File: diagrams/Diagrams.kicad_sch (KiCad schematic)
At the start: 16 parts

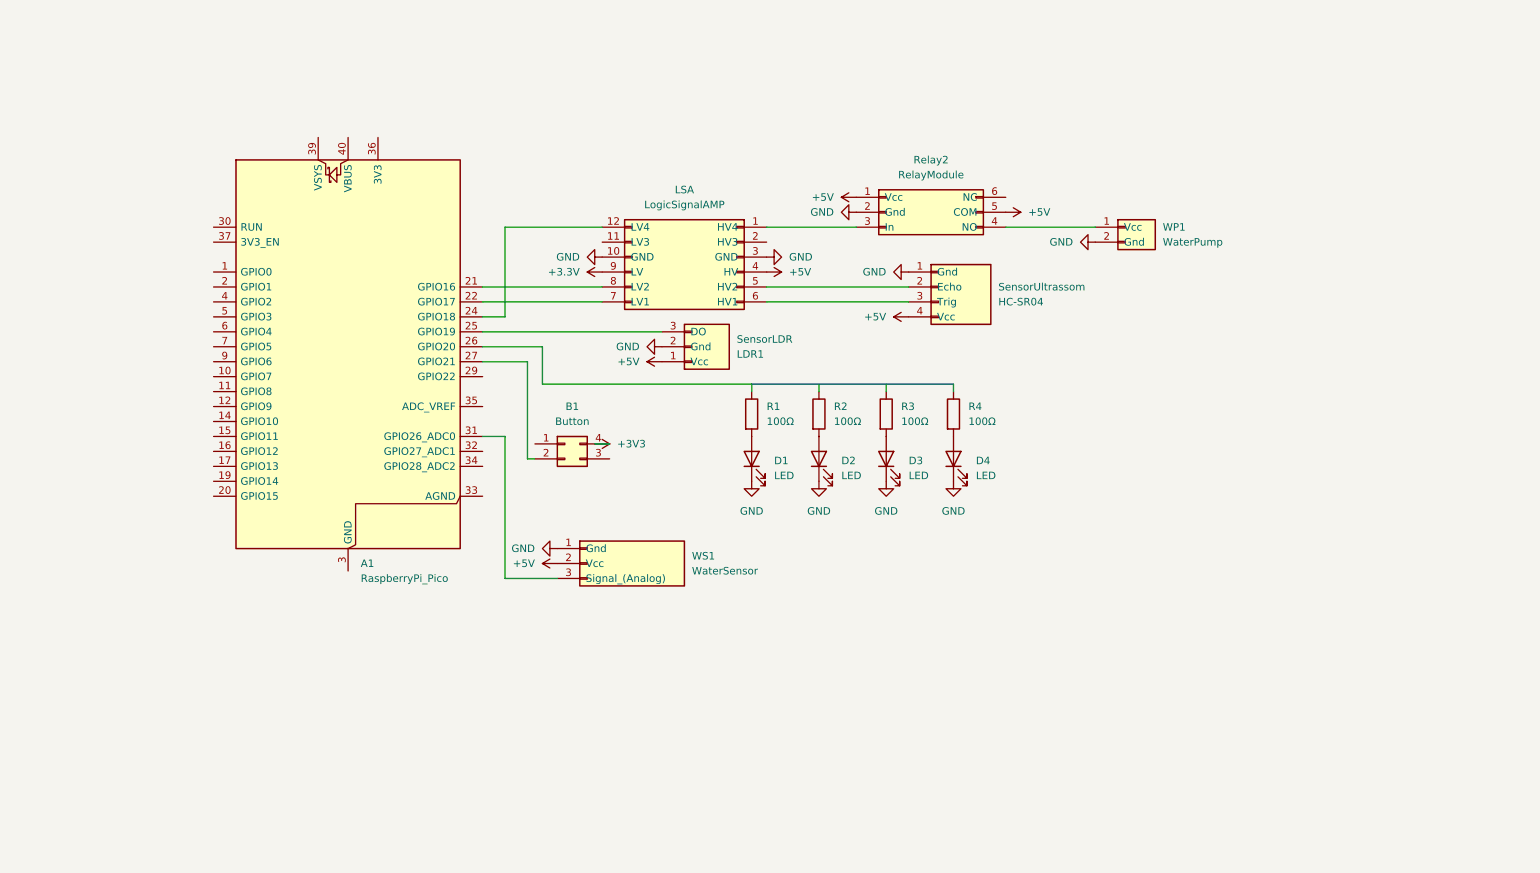
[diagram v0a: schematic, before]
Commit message: update: diagramas
- alterações pequenas no diagrama esquemático
- diagrama pcb inicial implementado
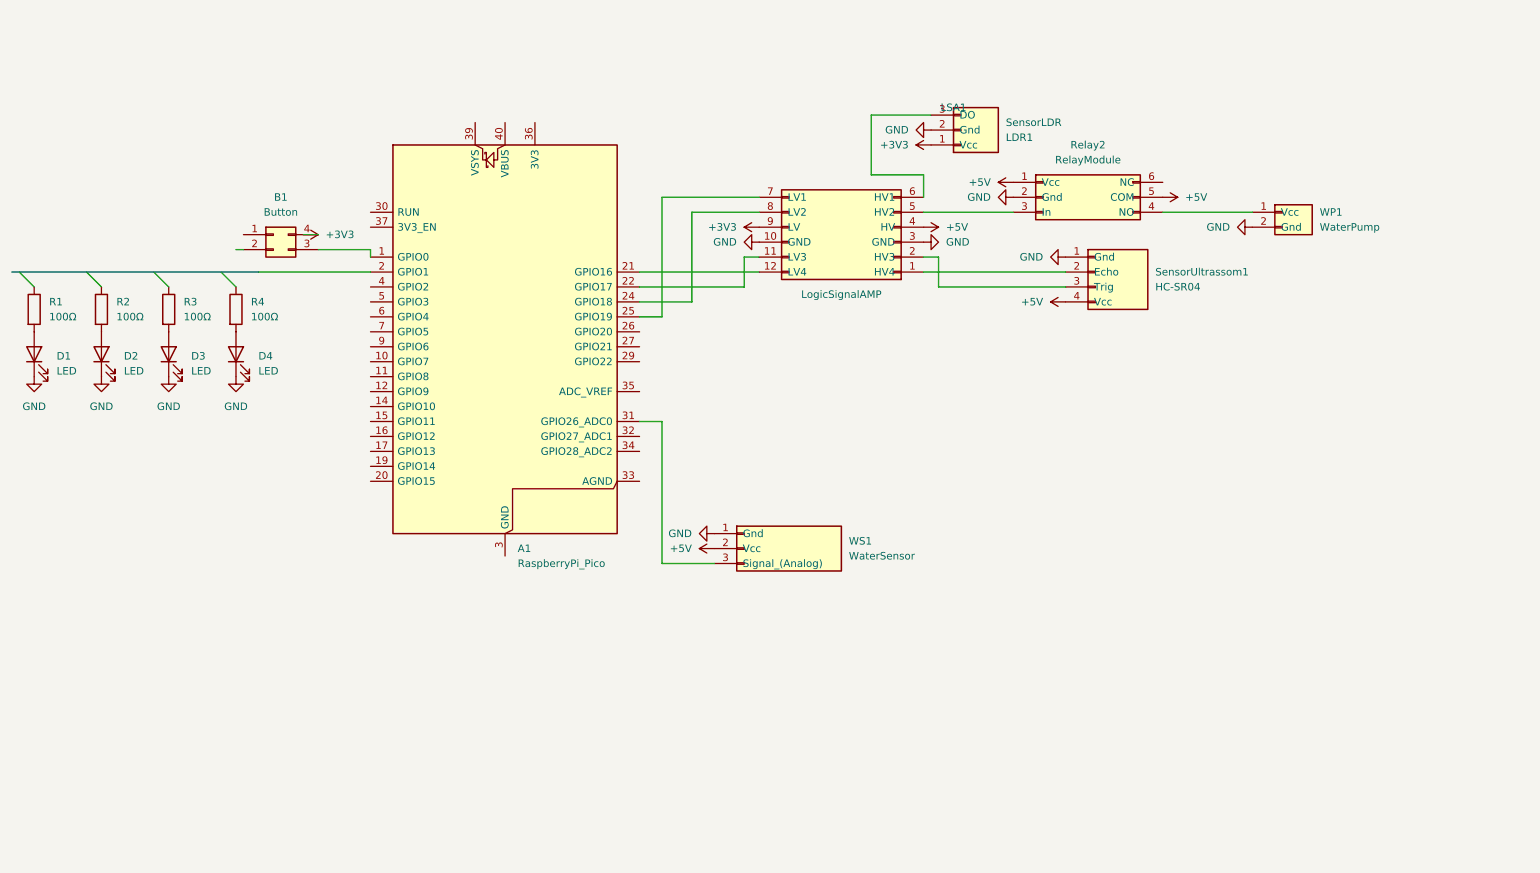
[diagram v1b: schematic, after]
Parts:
- renumbered LSA to LSA1, SensorUltrassom to SensorUltrassom1
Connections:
- net +3.3V is gone; now on net +3V3: LSA1.9 (LV)
- net +3V3: now also LDR1.1 (Vcc)
- net +5V: no longer LDR1.1 (Vcc)
- net at R1.1: no longer A1.26 (GPIO20)
- net at A1.1 (GPIO0): now also B1.3 (Pin_3)
- net at A1.21 (GPIO16): now also LSA1.12 (LV4); no longer LSA1.8 (LV2)
- net at A1.22 (GPIO17): now also LSA1.11 (LV3); no longer LSA1.7 (LV1)
- net at A1.24 (GPIO18): now also LSA1.8 (LV2); no longer LSA1.12 (LV4)
- net at A1.25 (GPIO19): now also LSA1.7 (LV1); no longer LDR1.3 (DO)
- net at A1.27 (GPIO21): no longer B1.2 (Pin_2)
- net at LSA1.1 (HV4): now also SensorUltrassom1.2 (Echo); no longer Relay2.3 (In)
- net at LSA1.2 (HV3): now also SensorUltrassom1.3 (Trig)
- net at LSA1.5 (HV2): now also Relay2.3 (In); no longer SensorUltrassom1.2 (Echo)
- net at LSA1.6 (HV1): now also LDR1.3 (DO); no longer SensorUltrassom1.3 (Trig)
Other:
- moved on the sheet: A1, B1, D1, D2, D3, D4, LDR1, LSA1, R1, R2, R3, R4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

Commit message: update: novo esquemático
- Esquemático refeito
- Nova biblioteca adicionada
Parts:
- removed LDR1: SensorLDR, symbol Connector_Generic:Conn_01x03
- added LDR: Conn_01x03_Socket, symbol Connector:Conn_01x03_Socket
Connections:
- net +5V: now also A1.40 (VBUS), LDR.1 (5V)
- net GND: now also A1.13 (GND), A1.18 (GND), A1.23 (GND), A1.28 (GND), A1.3 (GND), A1.38 (GND), A1.8 (GND), LDR.2 (GND)
- net HV1: now reaches LSA1.6 (HV1)
- net HV1: now also LDR.3 (LDR_SIGNAL)
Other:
- moved on the sheet: Relay2, SensorUltrassom1, WP1

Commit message: udpate: mais algumas mudanças
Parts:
- removed B1: Button, symbol Connector_Generic:Conn_02x02_Counter_Clockwise
- removed LDR: Conn_01x03_Socket, symbol Connector:Conn_01x03_Socket
- removed Relay2: RelayModule, symbol Connector_Generic:Conn_02x03_Counter_Clockwise
- removed SensorUltrassom1: HC-SR04, symbol Connector_Generic:Conn_01x04
- removed WP1: WaterPump, symbol Connector_Generic:Conn_01x02
- removed WS1: WaterSensor, symbol Connector_Generic:Conn_01x03
- added BTN1: BUTTON, symbol Biblio_EEN251:BUTTON
- added HC-SR1: HC-SR04, symbol Biblio_EEN251:HC-SR04
- added LDR1: LDR, symbol Biblio_EEN251:LDR
- added RELAY1: RELAY, symbol Biblio_EEN251:RELAY
- added WTR-SENS1: WATER-SENSOR, symbol Biblio_EEN251:WATER-SENSOR
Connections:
- net +3V3: now also A1.36 (3V3), BTN1.2 (IN)
- net +5V: now also HC-SR1.4 (VCC), LDR1.1 (VCC), RELAY1.1 (VCC), WTR-SENS1.2 (VCC)
- net GND: now also HC-SR1.1 (GND), LDR1.2 (GND), RELAY1.2 (GND), WTR-SENS1.1 (GND)
- net HV1: now also LDR1.3 (DO)
- net ADC0: now reaches A1.31 (GPIO26_ADC0)
- net ADC0: now also WTR-SENS1.3 (SIGNAL)
- net GPIO1: now reaches R4.1
- net GPIO1: now also A1.2 (GPIO1), R1.1, R2.1, R3.1
- net GPIO0: now reaches A1.1 (GPIO0)
- net GPIO0: now also BTN1.1 (VCC)
- net GPIO16: now reaches A1.21 (GPIO16), LSA1.12 (LV4)
- net GPIO17: now reaches A1.22 (GPIO17), LSA1.11 (LV3)
- net GPIO18: now reaches A1.24 (GPIO18), LSA1.8 (LV2)
- net GPIO19: now reaches A1.25 (GPIO19), LSA1.7 (LV1)
- net HV4: now reaches LSA1.1 (HV4)
- net HV4: now also HC-SR1.3 (TRIG)
- net HV3: now reaches LSA1.2 (HV3)
- net HV3: now also HC-SR1.2 (ECHO)
- net HV2: now reaches LSA1.5 (HV2)
- net HV2: now also RELAY1.3 (IN)

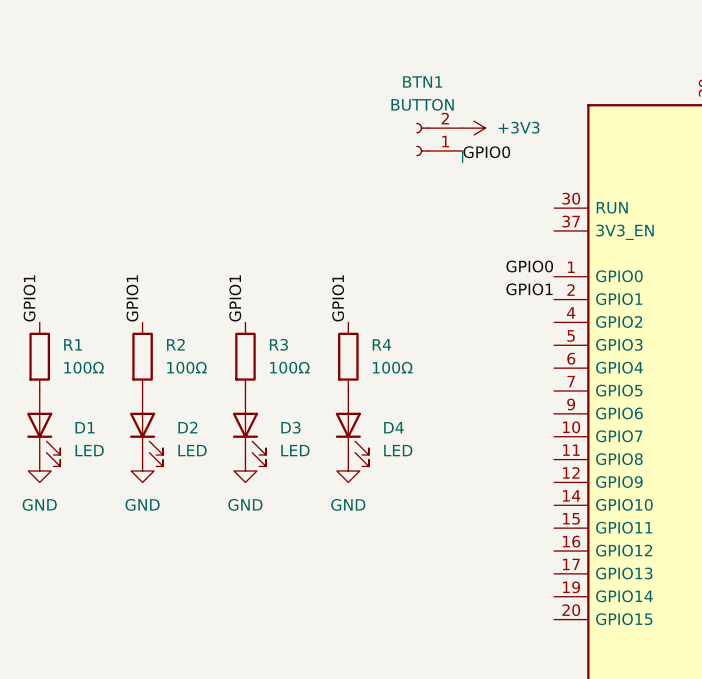
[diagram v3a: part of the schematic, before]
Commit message: update: atribuição de footprints básicas na schematic
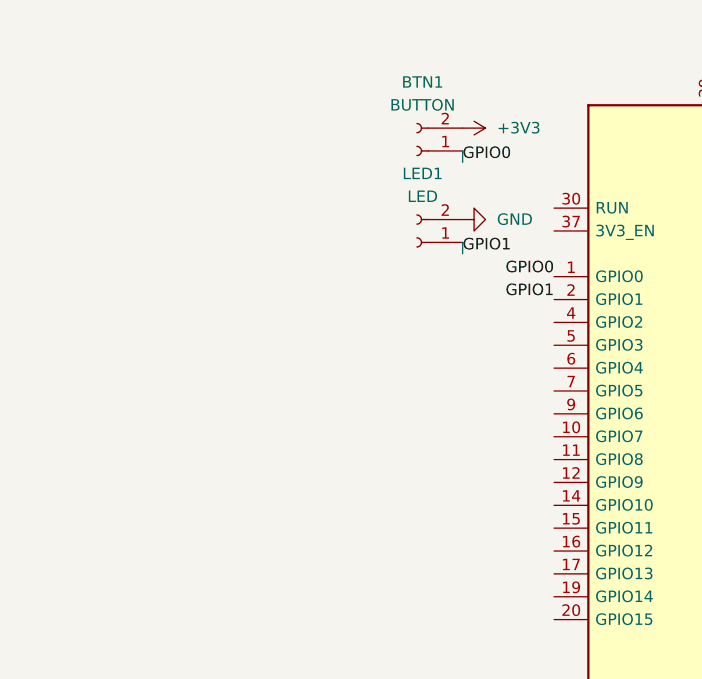
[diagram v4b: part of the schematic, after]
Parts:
- removed D1, D2, D3, D4: LED, symbol Device:LED
- removed R1, R2, R3, R4: 100Ω, symbol Device:R
- added LED1: LED, Connector_Wire:SolderWire-0.25sqmm_1x02_P4.2mm_D0.65mm_OD1.7mm, symbol Biblio_EEN251:LED
- BTN1: footprint (none) -> Connector_Wire:SolderWire-0.25sqmm_1x02_P4.2mm_D0.65mm_OD1.7mm
- HC-SR1: footprint (none) -> Connector_Wire:SolderWire-0.25sqmm_1x04_P4.2mm_D0.65mm_OD1.7mm
- LDR1, RELAY1, WTR-SENS1: footprint (none) -> Connector_Wire:SolderWire-0.25sqmm_1x03_P4.2mm_D0.65mm_OD1.7mm
- LSA1: footprint (none) -> Connector_PinHeader_2.54mm:PinHeader_2x06_P2.54mm_Horizontal
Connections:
- net GND: now also LED1.2 (VCC)
- net GPIO1: now also LED1.1 (GND)

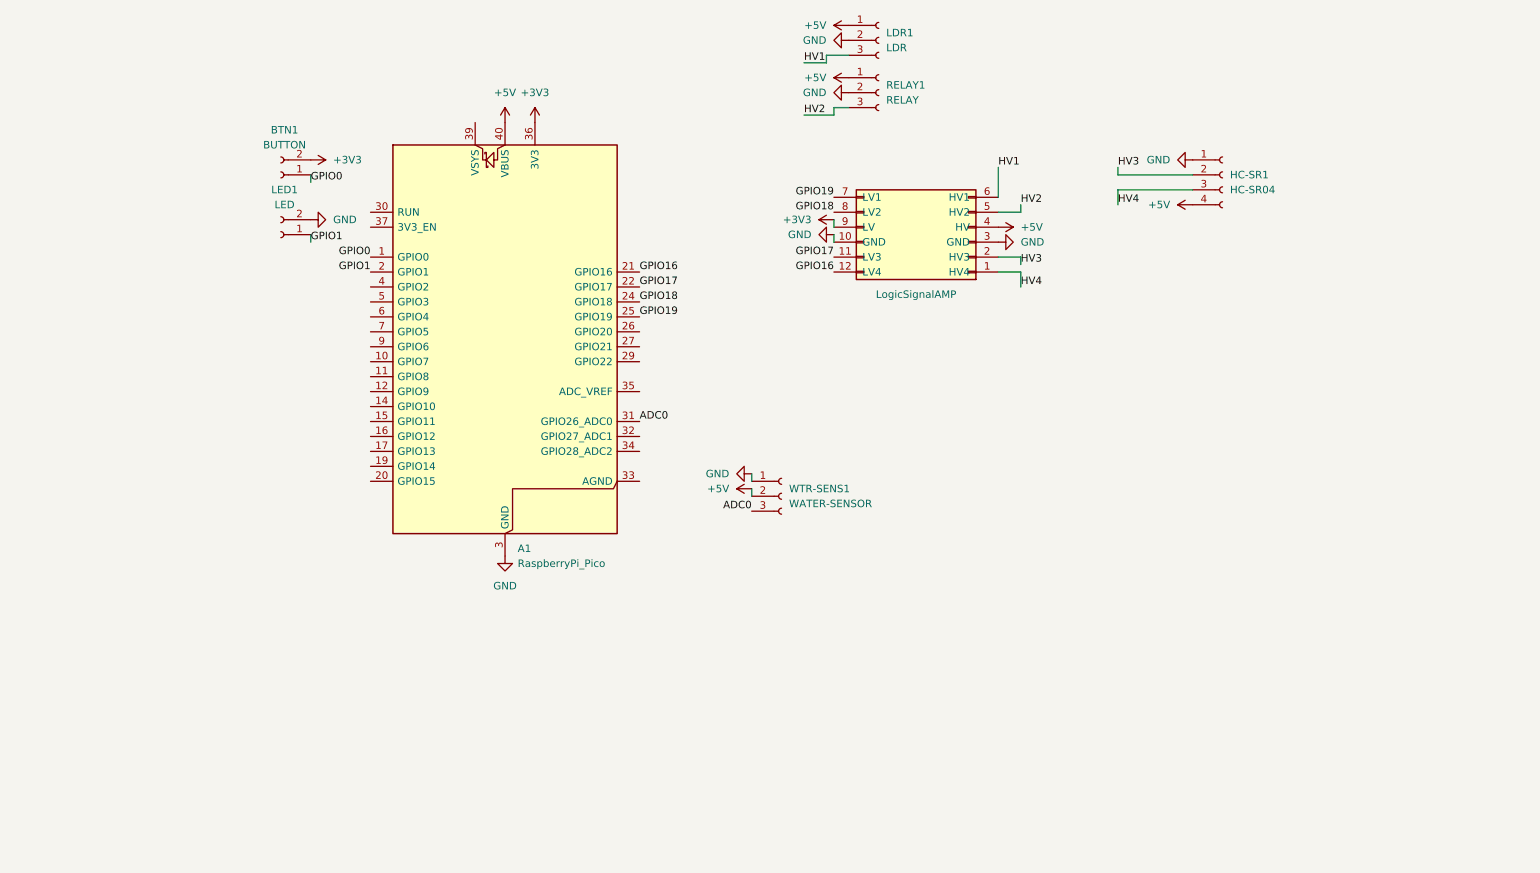
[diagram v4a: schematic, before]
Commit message: feat(pcb): finalizar layout da PCB pronto para impressão
- concluir roteamento da placa
- ajustar posicionamento dos módulos
- corrigir outline da PCB em Edge.Cuts
- prontificar PCB para fabricação/impressão
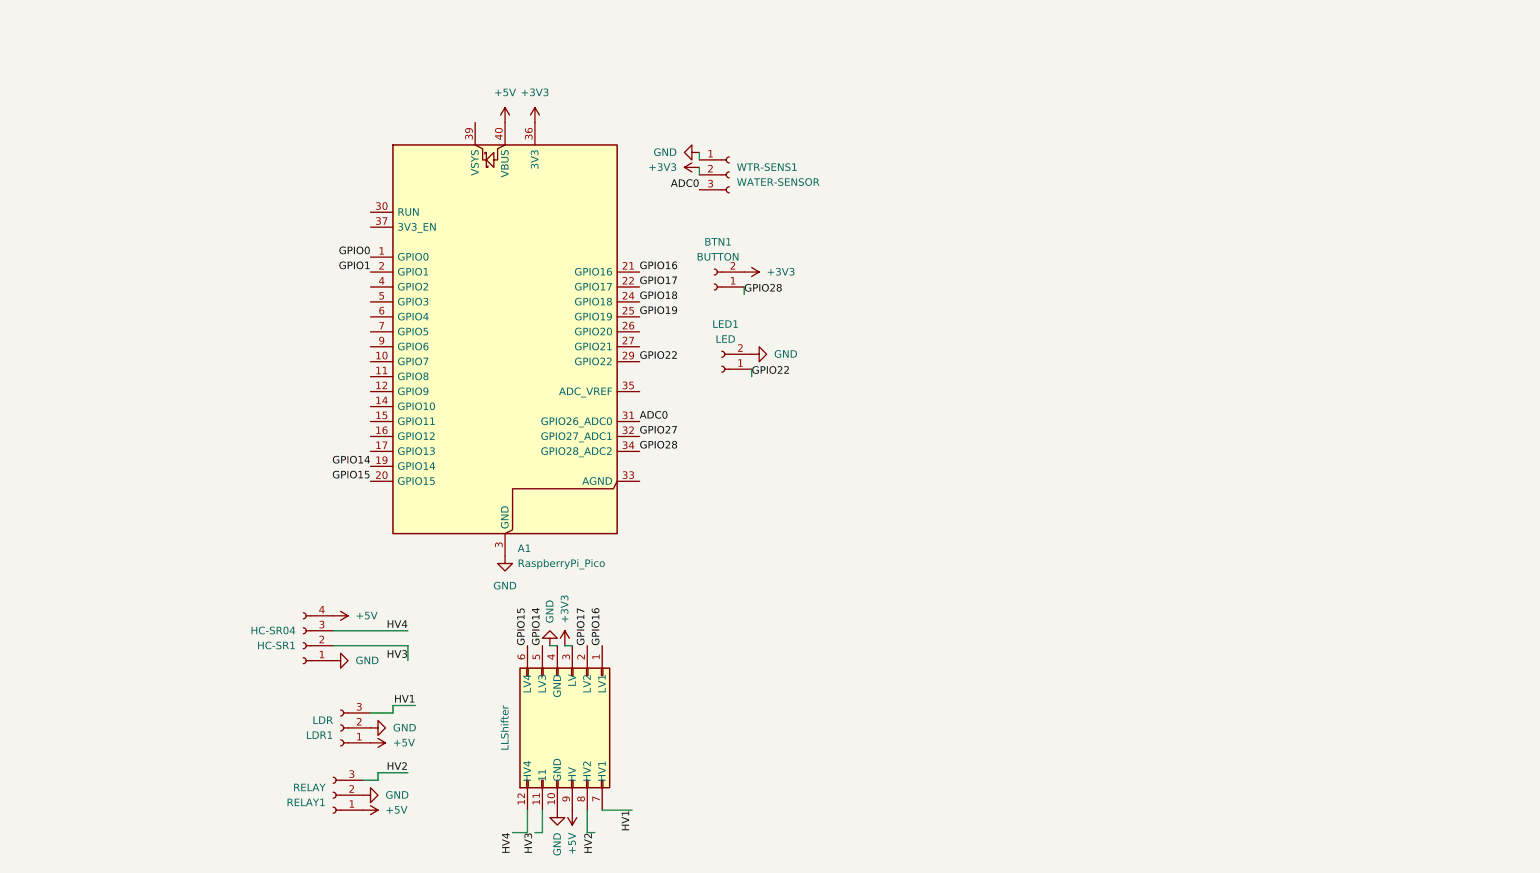
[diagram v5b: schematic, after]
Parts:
- LSA1: value LogicSignalAMP -> LLShifter; footprint Connector_PinHeader_2.54mm:PinHeader_2x06_P2.54mm_Horizontal -> Footprint-EEN251:LLShifer-Footprint; symbol Connector_Generic:Conn_02x06_Counter_Clockwise -> Biblio_EEN251:LOGIC-LEVEL-SHIFTER
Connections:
- net +3V3: now also LSA1.3 (LV), WTR-SENS1.2 (VCC); no longer LSA1.9 (LV)
- net +5V: now also LSA1.9 (HV); no longer LSA1.4 (HV), WTR-SENS1.2 (VCC)
- net GND: now also LSA1.4 (GND); no longer LSA1.3 (GND)
- net GPIO0: no longer BTN1.1 (VCC)
- net GPIO1: no longer LED1.1 (GND)
- net GPIO16: now also LSA1.1 (LV1); no longer LSA1.12 (LV4)
- net GPIO17: now also LSA1.2 (LV2); no longer LSA1.11 (LV3)
- net GPIO18: no longer LSA1.8 (LV2)
- net GPIO19: no longer LSA1.7 (LV1)
- net HV1: now also LSA1.7 (HV1); no longer LSA1.6 (HV1)
- net HV2: now also LSA1.8 (HV2); no longer LSA1.5 (HV2)
- net HV3: now also LSA1.11; no longer LSA1.2 (HV3)
- net HV4: now also LSA1.12 (HV4); no longer LSA1.1 (HV4)
- net GPIO14: now reaches A1.19 (GPIO14)
- net GPIO14: now also LSA1.5 (LV3)
- net GPIO15: now reaches A1.20 (GPIO15)
- net GPIO15: now also LSA1.6 (LV4)
- net GPIO22: now reaches A1.29 (GPIO22)
- net GPIO22: now also LED1.1 (GND)
- net GPIO27: now reaches A1.32 (GPIO27_ADC1)
- net GPIO28: now reaches A1.34 (GPIO28_ADC2)
- net GPIO28: now also BTN1.1 (VCC)
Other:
- moved on the sheet: BTN1, HC-SR1, LDR1, LED1, RELAY1, WTR-SENS1
